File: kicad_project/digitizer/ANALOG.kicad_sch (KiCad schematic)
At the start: 4 parts

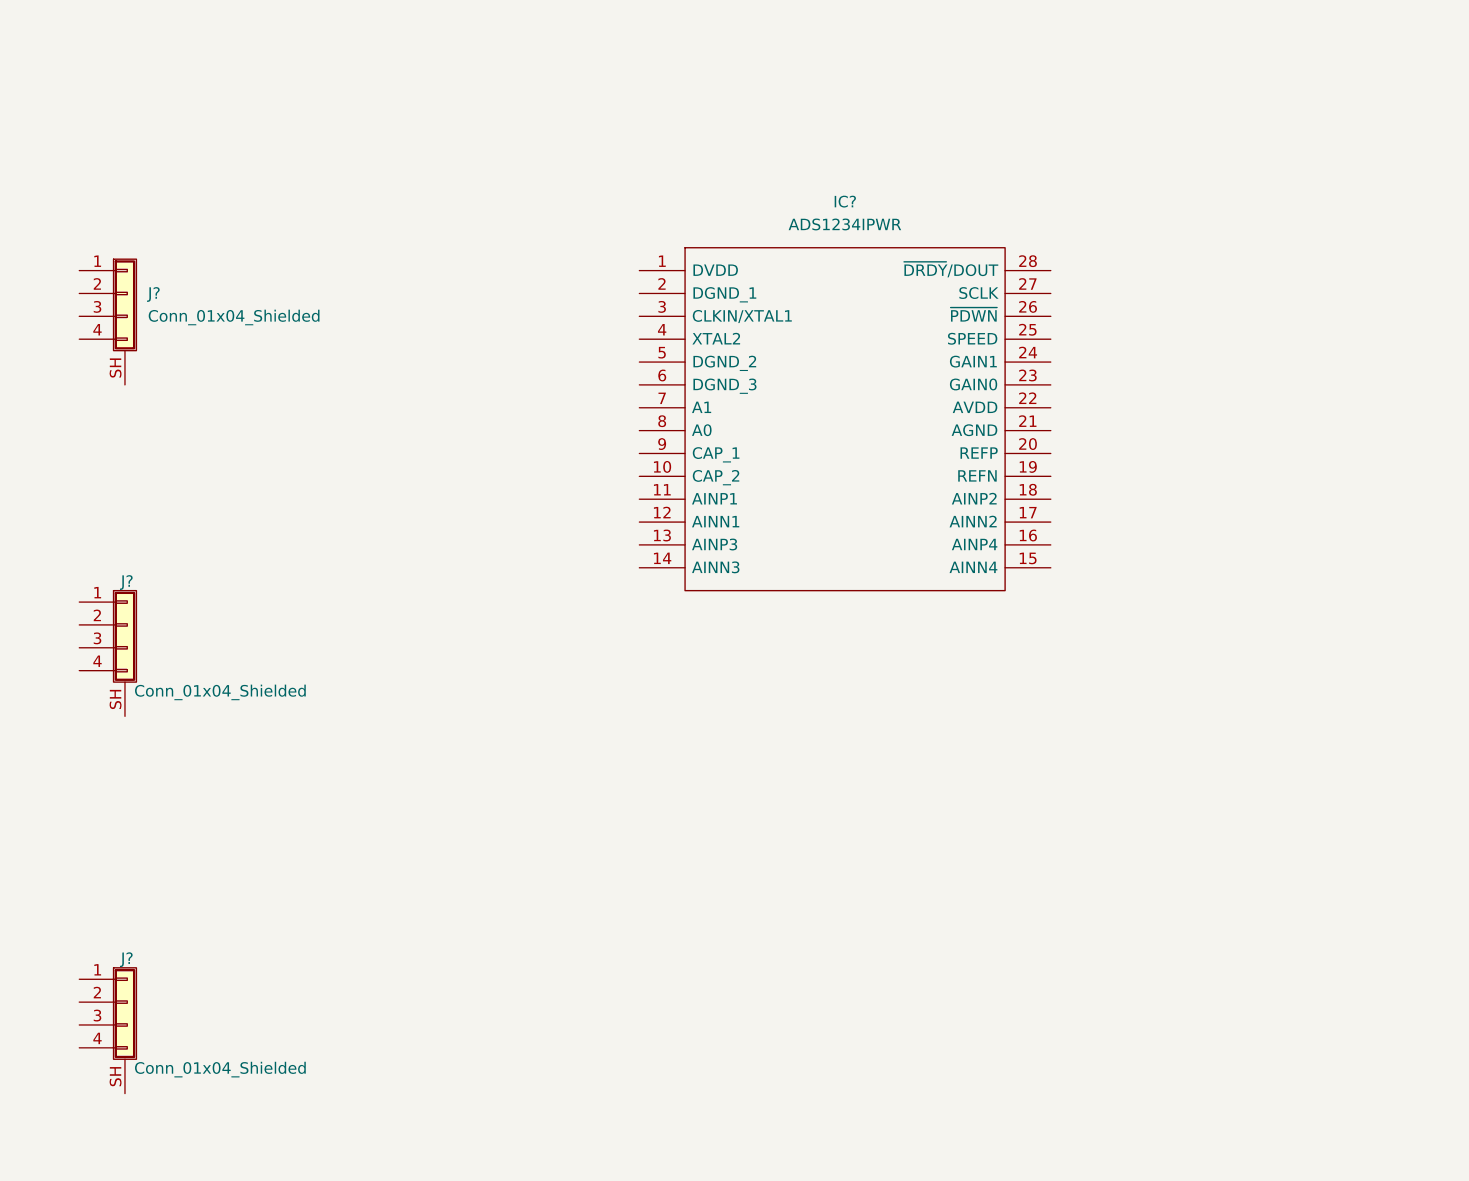
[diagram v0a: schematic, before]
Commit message: finished the CANPWR sheet, got to work on the MCU sheet (finished the CAN stuff). Good progress; still missing the MCU pin connections and the connector footprints (M12, deutsch, etc.)
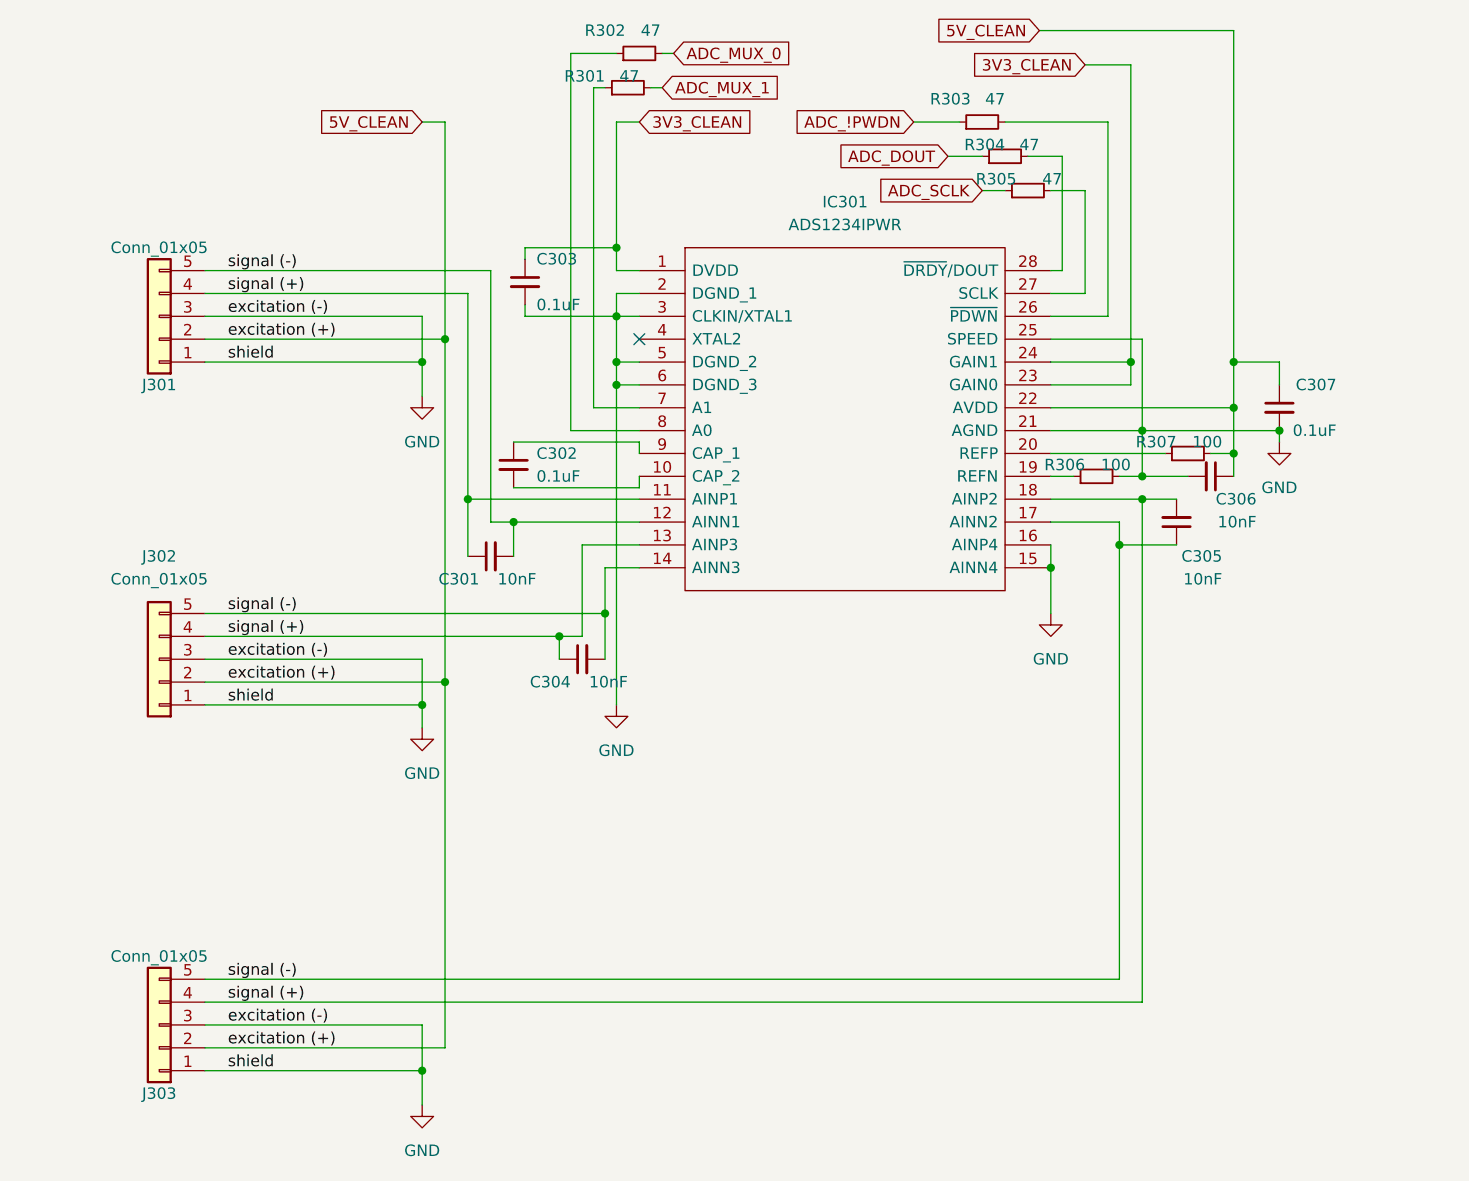
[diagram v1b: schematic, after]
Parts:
- removed J? (x3): Conn_01x04_Shielded, symbol Connector_Generic_Shielded:Conn_01x04_Shielded
- added C301, C304, C305, C306: 10nF, Capacitor_SMD:C_2220_5650Metric_Pad1.97x5.40mm_HandSolder, symbol Device:C_Small
- added C302, C303, C307: 0.1uF, Capacitor_SMD:C_2220_5650Metric_Pad1.97x5.40mm_HandSolder, symbol Device:C_Small
- added J301, J302, J303: Conn_01x05, symbol Connector_Generic:Conn_01x05
- added R301, R302, R303, R304, R305: 47, Resistor_SMD:R_2512_6332Metric_Pad1.40x3.35mm_HandSolder, symbol Device:R_Small
- added R306, R307: 100, Resistor_SMD:R_2512_6332Metric_Pad1.40x3.35mm_HandSolder, symbol Device:R_Small
- gave numbers to parts that had none: 1
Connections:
- net 3V3_CLEAN: now reaches IC301.1 (DVDD)
- net 3V3_CLEAN: now also IC301.23 (GAIN0), IC301.24 (GAIN1), C303.1
- net at IC301.10 (CAP_2): now also C302.2
- net signal (+): now reaches IC301.11 (AINP1)
- net signal (+): now also IC301.13 (AINP3), IC301.18 (AINP2), C301.1, C304.1, C305.2, J301.4 (Pin_4), J302.4 (Pin_4), J303.4 (Pin_4)
- net signal (-): now reaches IC301.12 (AINN1)
- net signal (-): now also IC301.14 (AINN3), IC301.17 (AINN2), C301.2, C304.2, C305.1, J301.5 (Pin_5), J302.5 (Pin_5), J303.5 (Pin_5)
- net GND: now reaches IC301.15 (AINN4)
- net GND: now also IC301.16 (AINP4), IC301.2 (DGND_1), IC301.21 (AGND), IC301.25 (SPEED), IC301.3 (CLKIN/XTAL1), IC301.5 (DGND_2), IC301.6 (DGND_3), C303.2, C306.2, C307.2, J301.1 (Pin_1), J301.3 (Pin_3), J302.1 (Pin_1), J302.3 (Pin_3), J303.1 (Pin_1), J303.3 (Pin_3), R306.2
- net at IC301.19 (REFN): now also R306.1
- net at IC301.20 (REFP): now also R307.1
- net 5V_CLEAN: now reaches IC301.22 (AVDD)
- net 5V_CLEAN: now also C306.1, C307.1, J301.2 (Pin_2), J302.2 (Pin_2), J303.2 (Pin_2), R307.2
- net at IC301.26 (~{PDWN}): now also R303.2
- net at IC301.27 (SCLK): now also R305.2
- net at IC301.28 (~{DRDY}/DOUT): now also R304.2
- net at IC301.7 (A1): now also R301.1
- net at IC301.8 (A0): now also R302.1
- net at IC301.9 (CAP_1): now also C302.1
- new net ADC_!PWDN: R303.1
- new net ADC_DOUT: R304.1
- new net ADC_MUX_0: R302.2
- new net ADC_MUX_1: R301.2
- new net ADC_SCLK: R305.1
- no-connect marks 0 -> 1

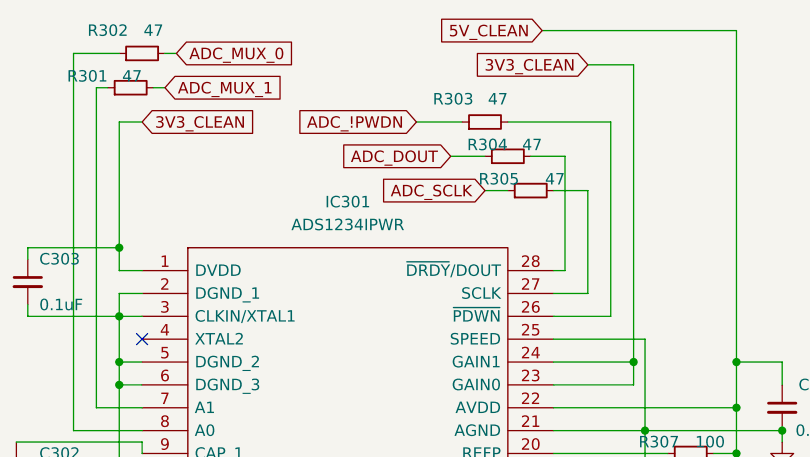
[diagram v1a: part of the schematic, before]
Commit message: connected the ADC I2C lines
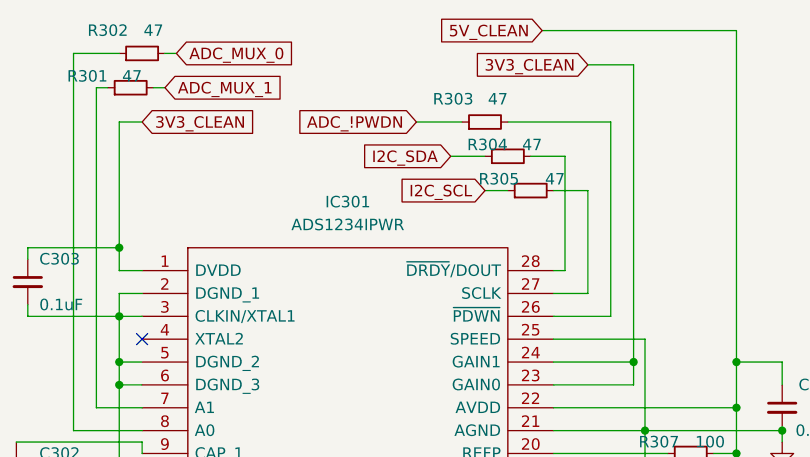
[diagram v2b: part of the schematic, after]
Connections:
- net ADC_DOUT renamed I2C_SDA
- net ADC_SCLK renamed I2C_SCL
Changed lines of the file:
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@@
     )
   )
-  (global_label "ADC_DOUT" (shape input) (at 144.78 39.37 180) (fields_autoplaced)
+  (global_label "I2C_SDA" (shape input) (at 144.78 39.37 180) (fields_autoplaced)
     (effects (font (size 1.27 1.27)) (justify right))
-    (property "Intersheet References" "${INTERSHEET_REFS}" (id 0) (at 132.8721 39.2906 0)
+    (property "Intersheet References" "${INTERSHEET_REFS}" (id 0) (at 134.7469 39.2906 0)
       (effects (font (size 1.27 1.27)) (justify right) hide)
     )
@@
     )
   )
-  (global_label "ADC_SCLK" (shape input) (at 148.59 43.18 180) (fields_autoplaced)
+  (global_label "I2C_SCL" (shape input) (at 148.59 43.18 180) (fields_autoplaced)
     (effects (font (size 1.27 1.27)) (justify right))
-    (property "Intersheet References" "${INTERSHEET_REFS}" (id 0) (at 136.8031 43.1006 0)
+    (property "Intersheet References" "${INTERSHEET_REFS}" (id 0) (at 138.6174 43.1006 0)
       (effects (font (size 1.27 1.27)) (justify right) hide)
     )

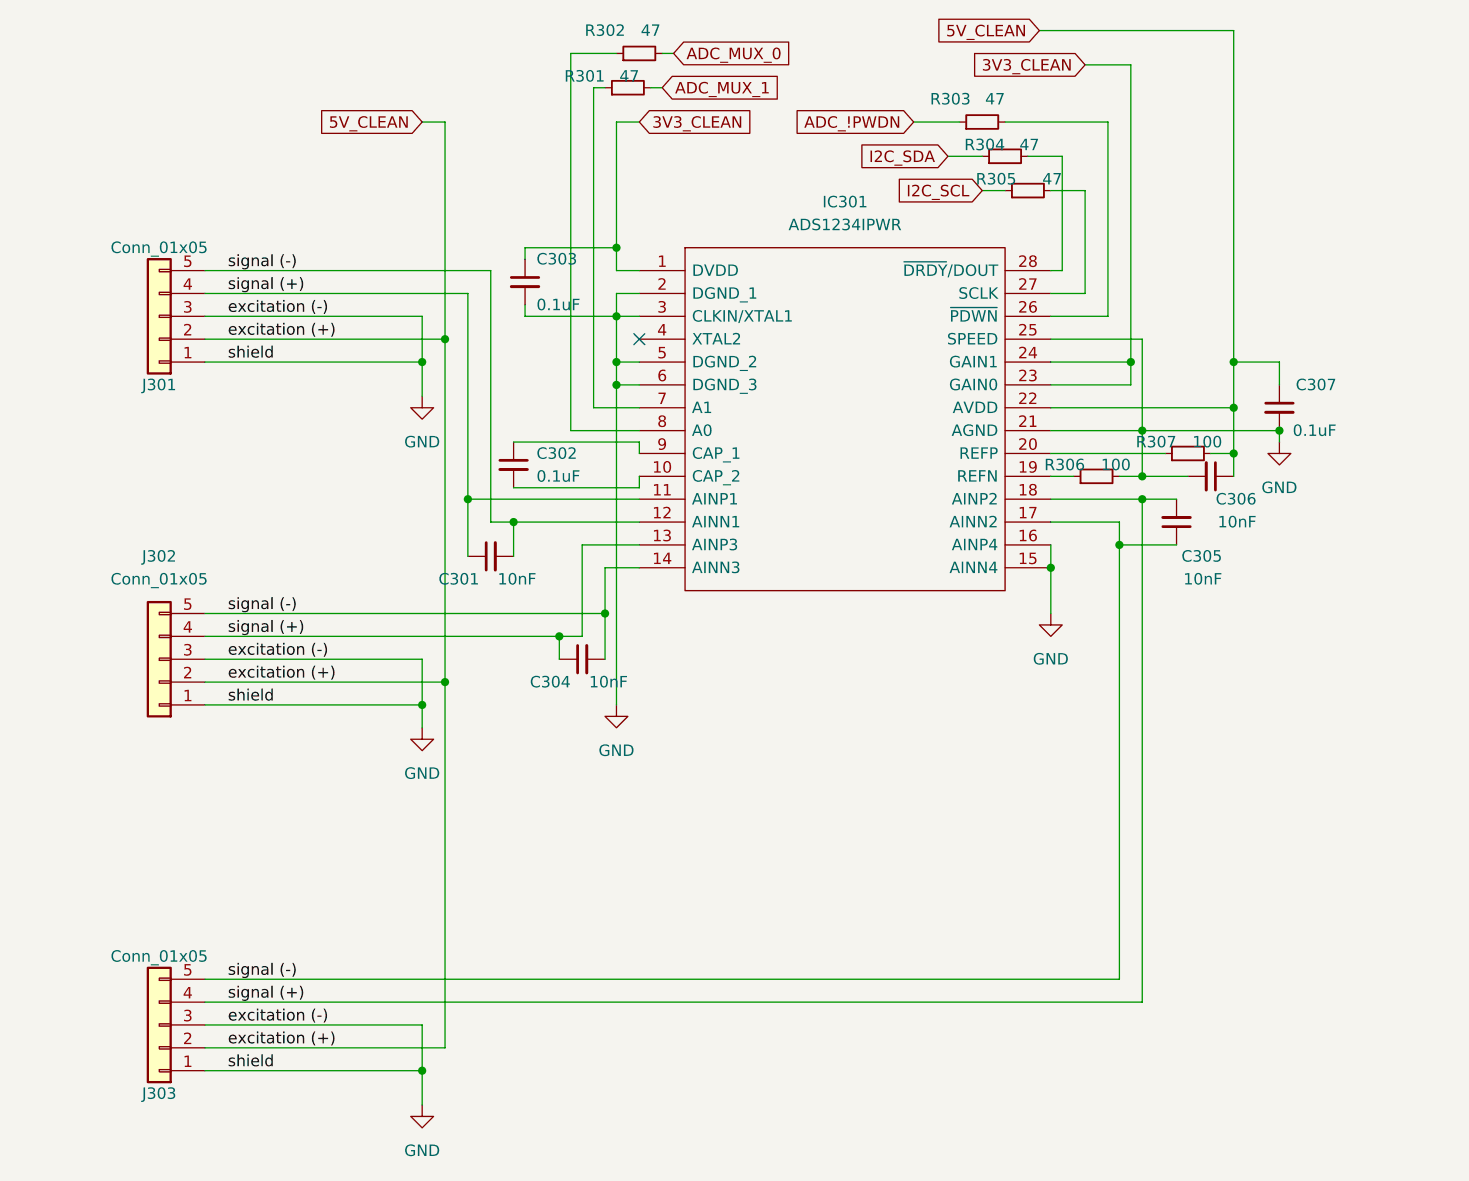
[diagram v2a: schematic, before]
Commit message: added GPIO lines, LED, other small changes
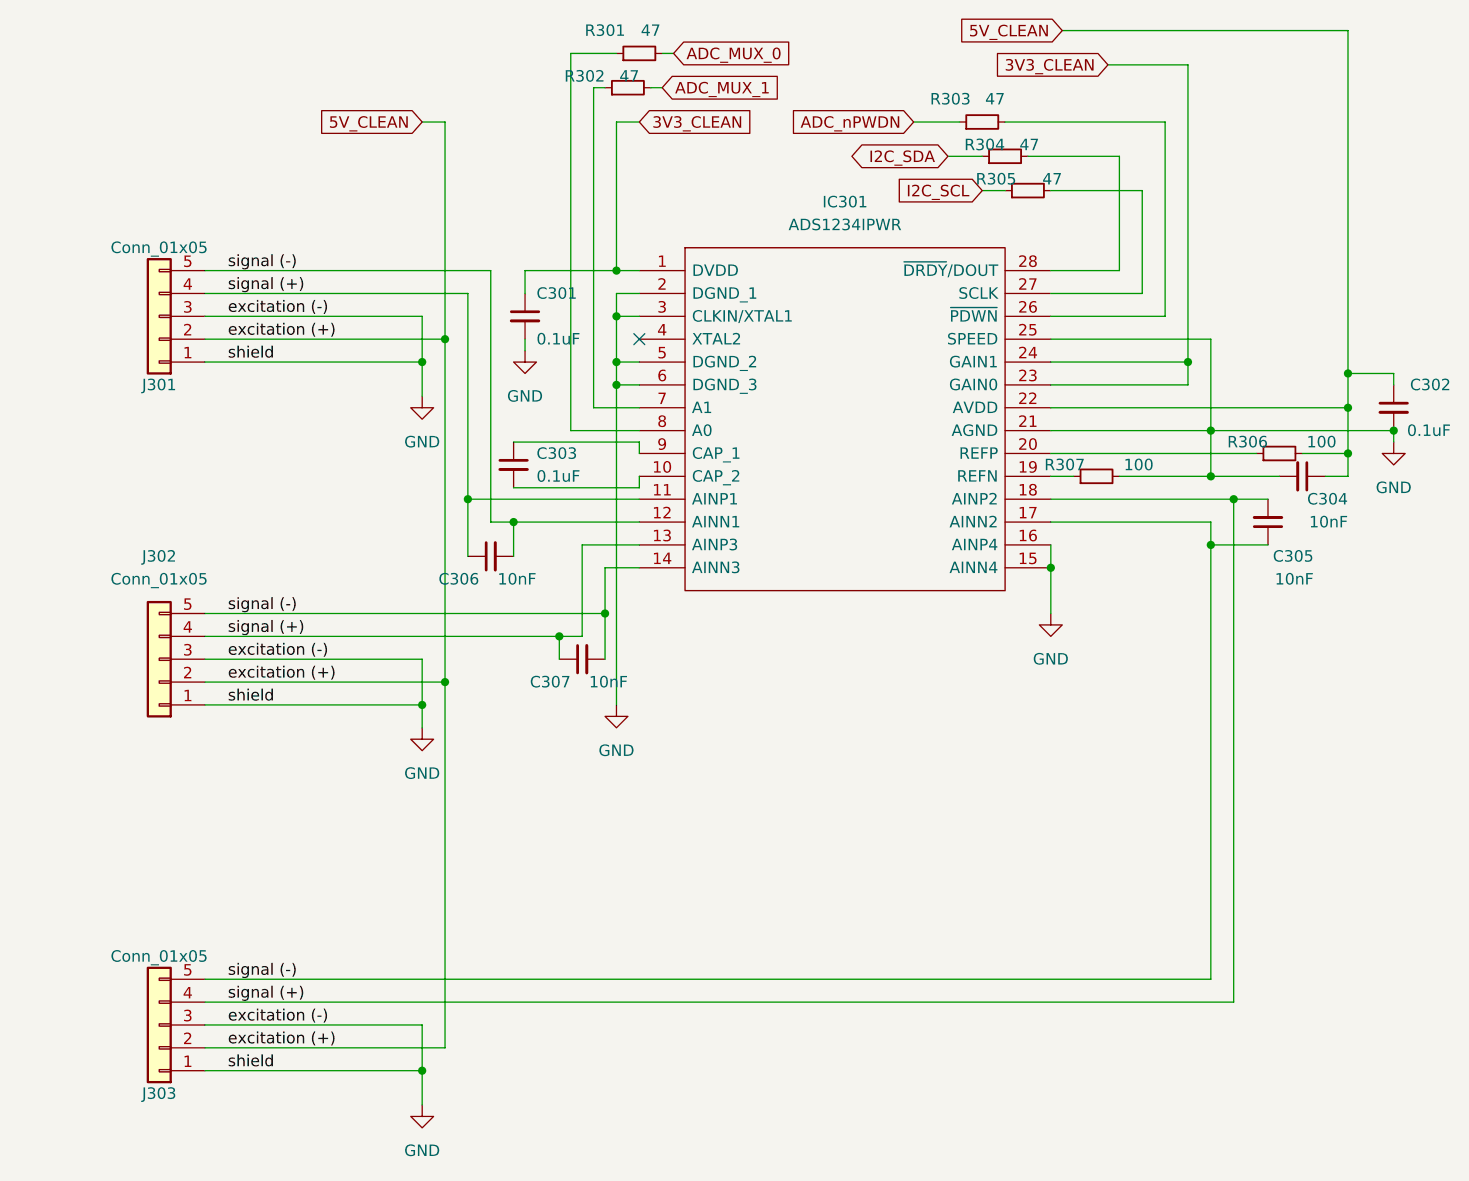
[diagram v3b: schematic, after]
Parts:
- renumbered C303 to C301, C307 to C302, C302 to C303, C306 to C304, C301 to C306, C304 to C307, R302 to R301, R301 to R302, R307 to R306, R306 to R307
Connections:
- net ADC_!PWDN renamed ADC_nPWDN
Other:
- moved on the sheet: C301, C302, C304, C305, R306

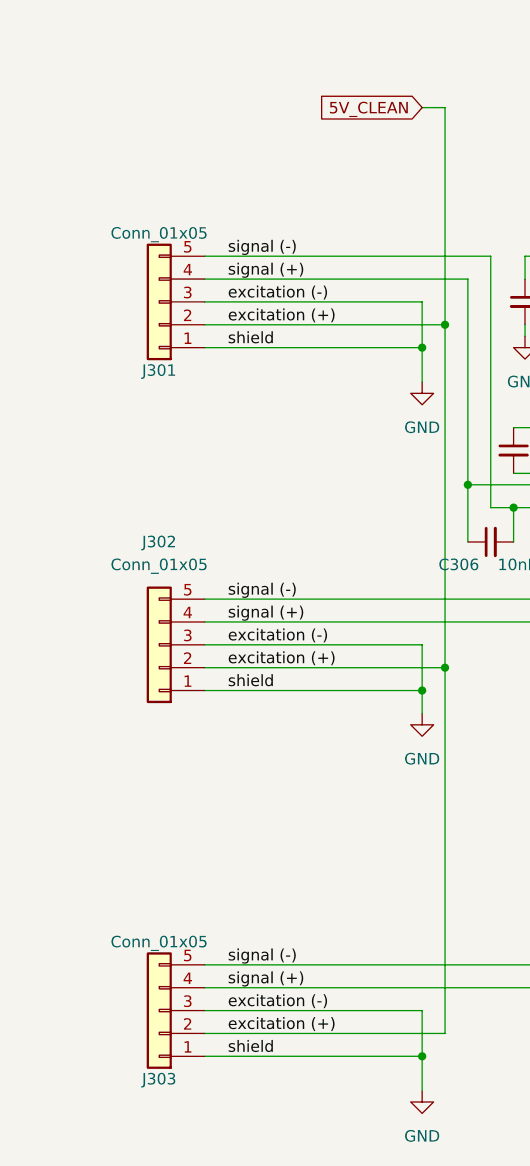
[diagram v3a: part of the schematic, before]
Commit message: added proper connector symbols and footprints for M12 and DT15 (digital upstream) connectors
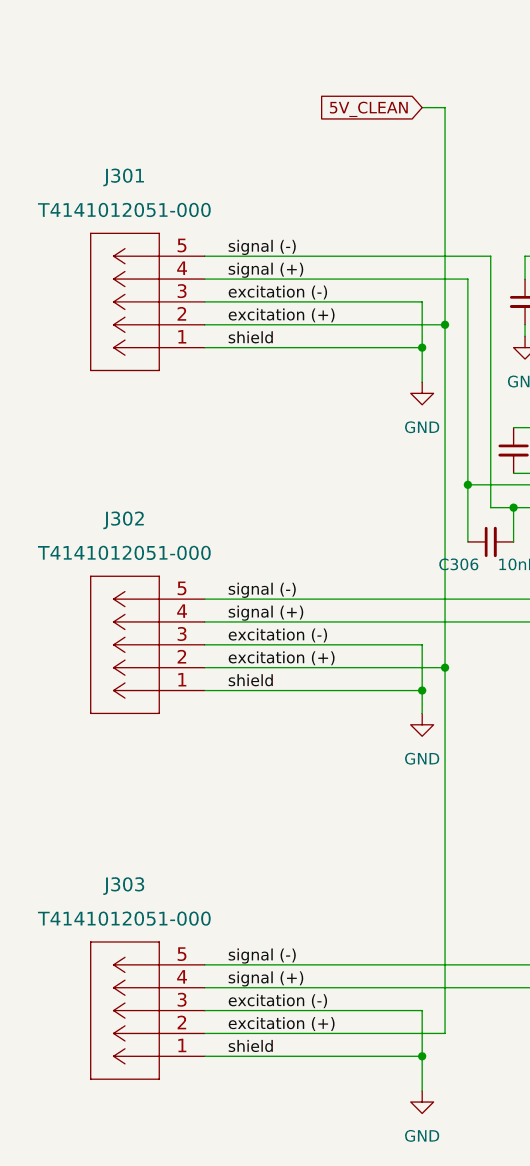
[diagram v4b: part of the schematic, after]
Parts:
- removed J301, J302, J303: Conn_01x05, symbol Connector_Generic:Conn_01x05
- added J301, J302, J303: T4141012051-000, CONN5_T4141012051, symbol 2022-01-31_01-29-15:T4141012051-000
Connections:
- net 5V_CLEAN: now also J301.2, J302.2, J303.2
- net GND: now also J301.1, J301.3, J302.1, J302.3, J303.1, J303.3
- net signal (+): now also J301.4, J302.4, J303.4
- net signal (-): now also J301.5, J302.5, J303.5
